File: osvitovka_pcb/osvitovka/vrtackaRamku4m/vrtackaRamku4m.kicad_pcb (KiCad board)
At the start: 2 copper layers, 21 parts, among them J1 Screw_Terminal_01x01, J2 Screw_Terminal_01x01, J3 M+, J4 M-, K1 RSM822, Q1 BC817, U1 LM78M05_TO220

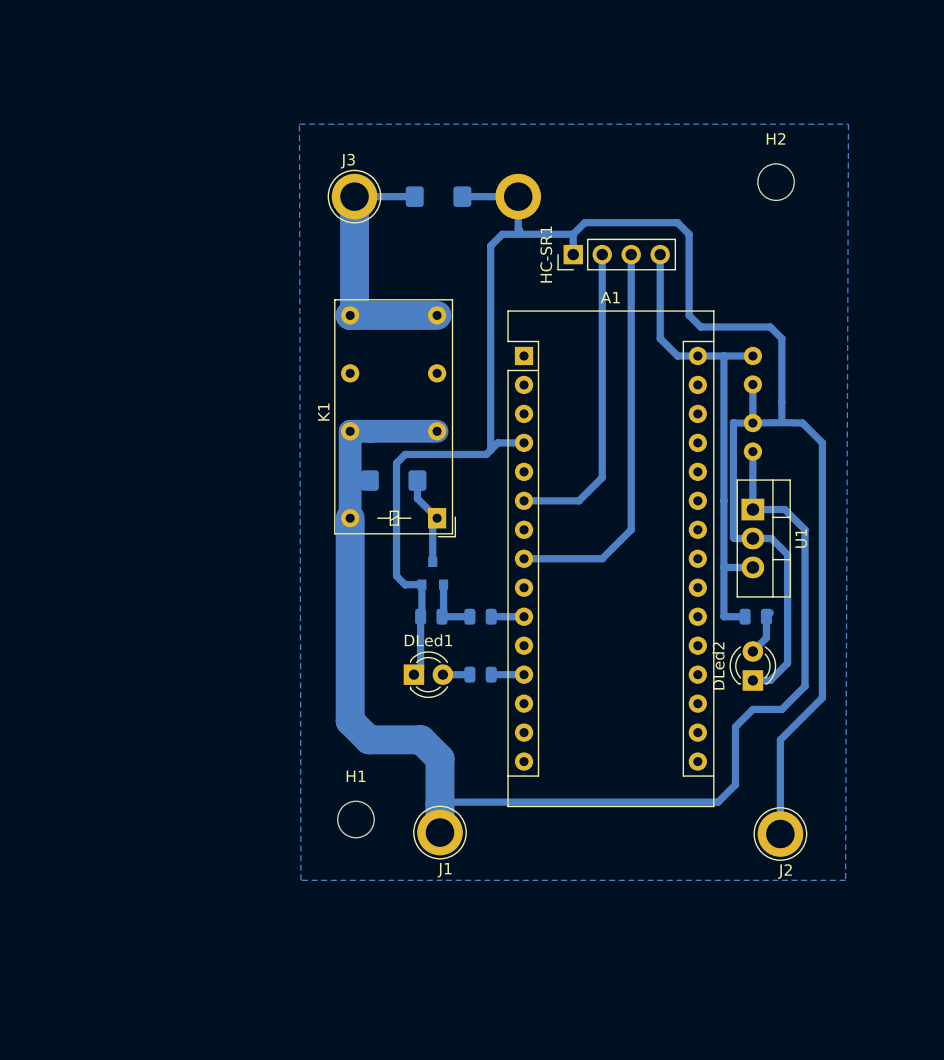
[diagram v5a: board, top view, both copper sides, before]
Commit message: Totálně předělaný plošňák. Zvětšené plošky, širší cestičky. Založena vlastní knihovna.
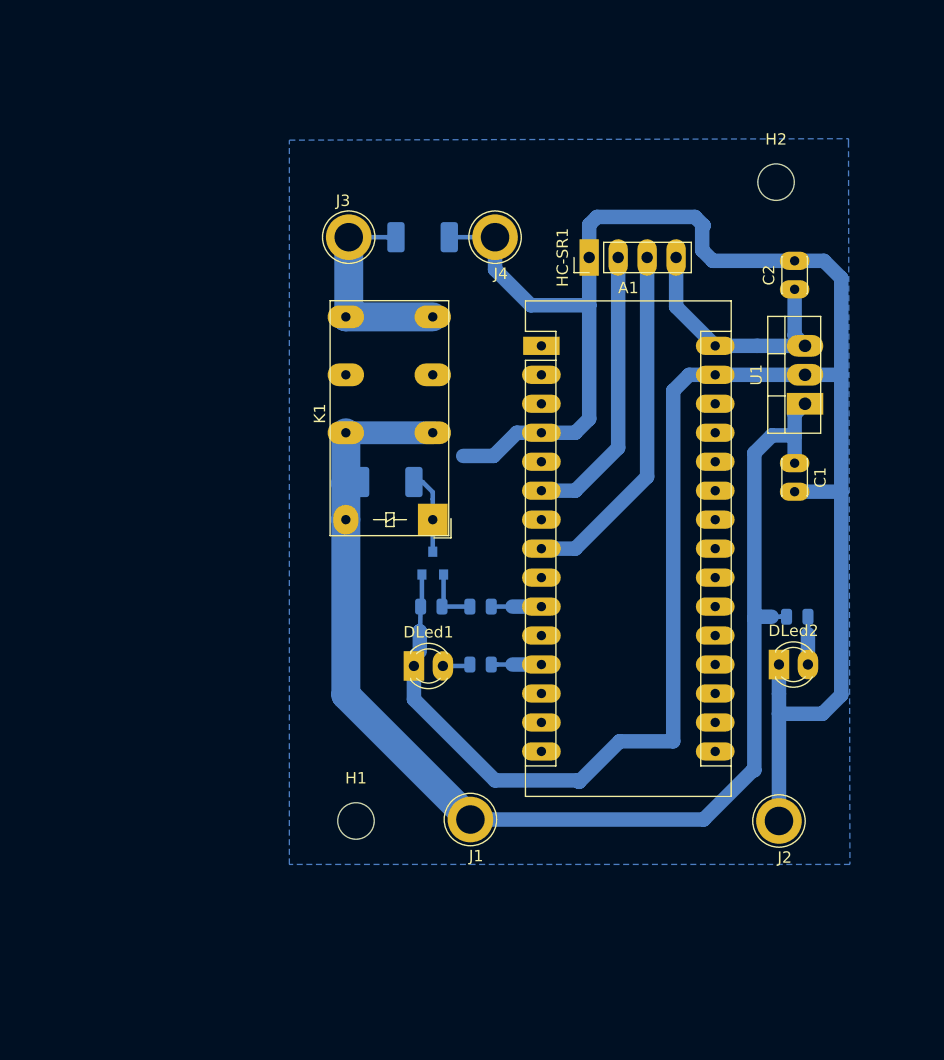
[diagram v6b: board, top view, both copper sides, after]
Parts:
- A1: footprint Module:Arduino_Nano -> LPouzdra:Arduino_Nano_vetsi_plosky
- C1, C2: footprint Capacitor_THT:C_Disc_D3.0mm_W2.0mm_P2.50mm -> LPouzdra:AR_C_Disc_D3.0mm_W2.0mm_P2.50mm; moved to F.Cu
- D1, D2: footprint Diode_SMD:D_1806_4516Metric_Pad1.57x1.80mm_HandSolder -> Diode_SMD:D_2010_5025Metric_Pad1.52x2.65mm_HandSolder
- DLed1, DLed2: footprint LED_THT:LED_D3.0mm -> LPouzdra:AR_LED_D3.0mm
- HC-SR1: footprint Connector_PinHeader_2.54mm:PinHeader_1x04_P2.54mm_Vertical -> LPouzdra:AR_PinHeader_1x04_P2.54mm_Vertical
- J4: moved to F.Cu
- K1: footprint Relay_THT:Relay_DPDT_Finder_30.22 -> LPouzdra:AR_Relay_DPDT_Finder_30.22
- U1: footprint Package_TO_SOT_THT:TO-220-3_Vertical -> LPouzdra:AR_TO-220-3_Vertical
- moved U1 10.3 mm to (170.2, 75.3), turned to 90 degrees
- moved C2 6.89 mm to (169.3, 65.3), turned to 90 degrees
- moved J4 4.10 mm to (143.0, 60.7)
- moved D2 3.82 mm to (136.7, 60.7)
- moved C1 3.80 mm to (169.3, 80.5), turned to 270 degrees
- moved R4 3.63 mm to (169.5, 94.0)
- moved J3 3.59 mm to (130.2, 60.7)
- moved J1 2.90 mm to (140.8, 111.8)
- moved DLed2 2.68 mm to (167.9, 98.2), turned to 0 degrees
- moved A1 1.76 mm to (147.1, 70.2)
- moved HC-SR1 1.42 mm to (151.3, 62.5)
- moved J2 1.15 mm to (167.9, 111.9)
- moved R1 0.89 mm to (141.7, 93.1)
- moved R2 0.89 mm to (137.4, 93.1)
- moved Q1 0.89 mm to (137.5, 89.3)
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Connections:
- A1 pad 29: Net-(A1-Pad29) -> GND
- R4 pad 2: +5V -> +12V
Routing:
- net GND: track 179.0 -> 218.2 mm
- net +5V: track 43.4 -> 22.4 mm
- net Net-(D2-Pad1): track 23.5 -> 18.8 mm
- net Trig: track 34.6 -> 31.1 mm
- net Echo: track 27.3 -> 25.0 mm
- net PWM1: track 2.87 -> 4.40 mm
- net Led_yellow: track 2.87 -> 4.40 mm
- net Net-(D1-Pad2): track 8.00 -> 7.24 mm
- net +12V: track 113.9 -> 114.5 mm
